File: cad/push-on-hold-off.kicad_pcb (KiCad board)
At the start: 2 copper layers, 22.9 x 12.7 mm, 17 parts, among them P1 CONN_01X04, P2 CONN_01X04, Q1 IRF7309IPBF, SW1 SW_PUSH_SMALL

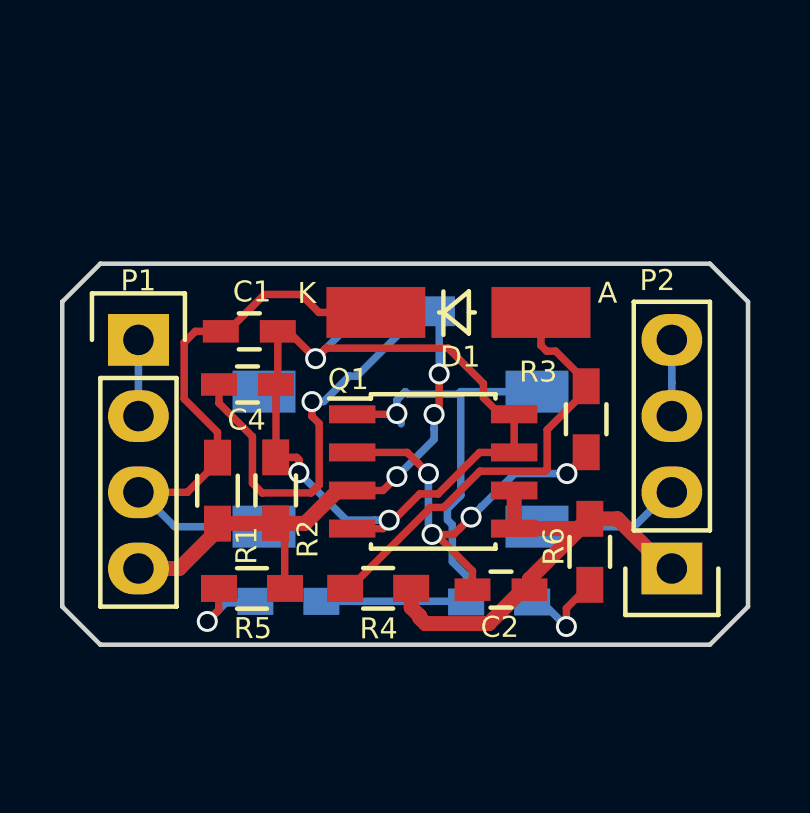
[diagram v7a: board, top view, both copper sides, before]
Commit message: Fix auto-on jumper which was supposed to be to ground
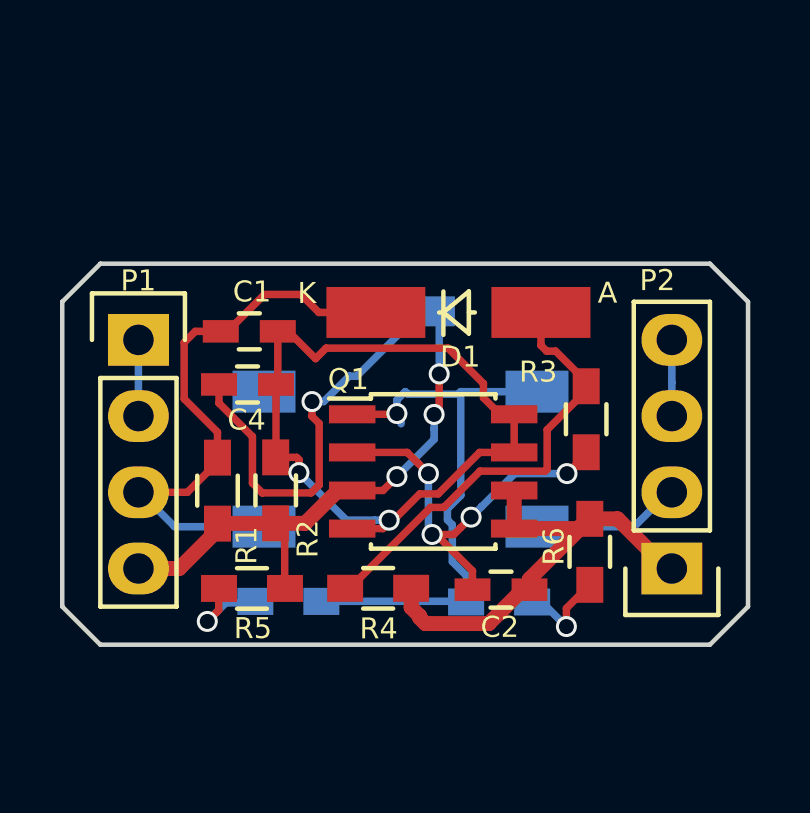
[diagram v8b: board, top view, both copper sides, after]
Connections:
- JP1 pad 1: Net-(C1-Pad1) -> GND
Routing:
- net Net-(C1-Pad1): track 28.8 -> 26.5 mm, vias 3 -> 2
- net GND: track 25.2 -> 26.0 mm
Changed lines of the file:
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@@
-(kicad_pcb (version 4) (host pcbnew 4.1.0-alpha+201606061201+6885~45~ubuntu14.04.1-product)
+(kicad_pcb (version 4) (host pcbnew 4.1.0-alpha+201606291451+6956~45~ubuntu14.04.1-product)
   (general
     (links 38)
@@
     (thickness 1.6)
     (drawings 20)
-    (tracks 199)
+    (tracks 197)
     (zones 0)
     (modules 17)
@@
   )
   (setup
-    (last_trace_width 0.25)
+    (last_trace_width 0.1)
     (user_trace_width 0.1)
     (user_trace_width 0.2)
@@
     (pad_to_mask_clearance 0.2)
     (aux_axis_origin 0 0)
-    (grid_origin 217.175 100.345)
+    (grid_origin 225.815 102.355)
     (visible_elements 7FFEFFFF)
     (pcbplotparams
@@
     (fp_arc (start -0.954 0) (end -0.954 -1.016) (angle -90) (layer B.SilkS) (width 0.2032))
     (pad 1 smd rect (at -1.35 0) (size 1 1) (layers B.Cu B.Paste B.Mask)
-      (net 1 "Net-(C1-Pad1)"))
+      (net 6 GND))
     (pad 3 smd rect (at 1.35 0) (size 1 1) (layers B.Cu B.Paste B.Mask)
       (net 7 /Vin))
@@
   (segment (start 223.085 102.585) (end 223.435 102.585) (width 0.25) (layer F.Cu) (net 1))
   (segment (start 223.435 102.585) (end 224.345 103.495) (width 0.25) (layer F.Cu) (net 1))
-  (segment (start 224.345 103.495) (end 225.445 102.395) (width 0.25) (layer B.Cu) (net 1))
-  (via (at 224.345 103.495) (size 0.7) (drill 0.5) (layers F.Cu B.Cu) (net 1))
-  (segment (start 225.445 102.395) (end 225.445 102.035) (width 0.25) (layer B.Cu) (net 1))
-  (segment (start 225.445 102.035) (end 225.785 101.915) (width 0.25) (layer B.Cu) (net 1))
   (segment (start 223.025 104.355) (end 223.025 106.775) (width 0.25) (layer F.Cu) (net 1))
   (segment (start 223.025 106.775) (end 223.015 106.785) (width 0.25) (layer F.Cu) (net 1))
@@
   (segment (start 231.85582 101.955) (end 231.85582 103.05463) (width 0.25) (layer F.Cu) (net 5))
   (segment (start 231.85582 103.05463) (end 232.04619 103.245) (width 0.25) (layer F.Cu) (net 5))
+  (segment (start 225.445 102.395) (end 225.445 102.035) (width 0.25) (layer B.Cu) (net 6))
+  (segment (start 225.445 102.035) (end 225.785 101.915) (width 0.25) (layer B.Cu) (net 6))
   (segment (start 236.22 105.41) (end 236.22 104.2964) (width 0.25) (layer B.Cu) (net 6))
   (segment (start 236.22 104.2964) (end 236.22 102.87) (width 0.25) (layer B.Cu) (net 6))
@@
       (pts
         (xy 238.765 101.615) (xy 238.765 111.775) (xy 237.495 113.045) (xy 217.175 113.045) (xy 215.905 111.775)
-        (xy 215.905 101.615) (xy 217.175 100.345) (xy 237.495 100.345) (xy 238.765 101.615)
+        (xy 215.905 101.615) (xy 217.175 100.345) (xy 237.495 100.345)
       )
     )
@@
       (pts
         (xy 238.765 101.615) (xy 238.765 111.775) (xy 237.495 113.045) (xy 217.175 113.045) (xy 215.905 111.775)
-        (xy 215.905 101.615) (xy 217.175 100.345) (xy 237.495 100.345) (xy 238.765 101.615)
+        (xy 215.905 101.615) (xy 217.175 100.345) (xy 237.495 100.345)
       )
     )
